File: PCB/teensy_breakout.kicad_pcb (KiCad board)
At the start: 2 copper layers, 88 x 68 mm, 59 parts, among them J1 Conn_01x02_Male, J10 3-way_power_jumper, J11 3-way_power_jumper, J12 Conn_01x06_Male, J13 Conn_01x06_Male, J14 Conn_01x06_Male, J15 Conn_01x06_Male, J16 3-way_power_jumper, J17 3-way_power_jumper, J18 Conn_01x06_Male, J19 Conn_01x06_Male, J2 Conn_01x03_Male, J20 Conn_01x06_Male, J21 Conn_01x06_Male, J22 3-way_power_jumper, J23 3-way_power_jumper, J24 Conn_01x03_Male, J25 Conn_01x03_Male, J26 Conn_01x03_Male, J27 Conn_01x03_Male, J28 Conn_01x06_Male, J29 Conn_01x03_Male, J3 Conn_01x03_Male, J30 Conn_01x03_Male, J31 Conn_01x03_Male, J32 Conn_01x03_Male, J33 Conn_01x03_Male, J35 Conn_01x03_Male, J36 Conn_01x03_Male, J4 Conn_01x04_Male, J5 Conn_01x04_Male, J6 Conn_01x03_Male, J7 Conn_01x02_Male, J8 Conn_01x04_Male, J9 Conn_01x04_Male, U1 Teensy4.0, U2 Pololu_D24V22Fx

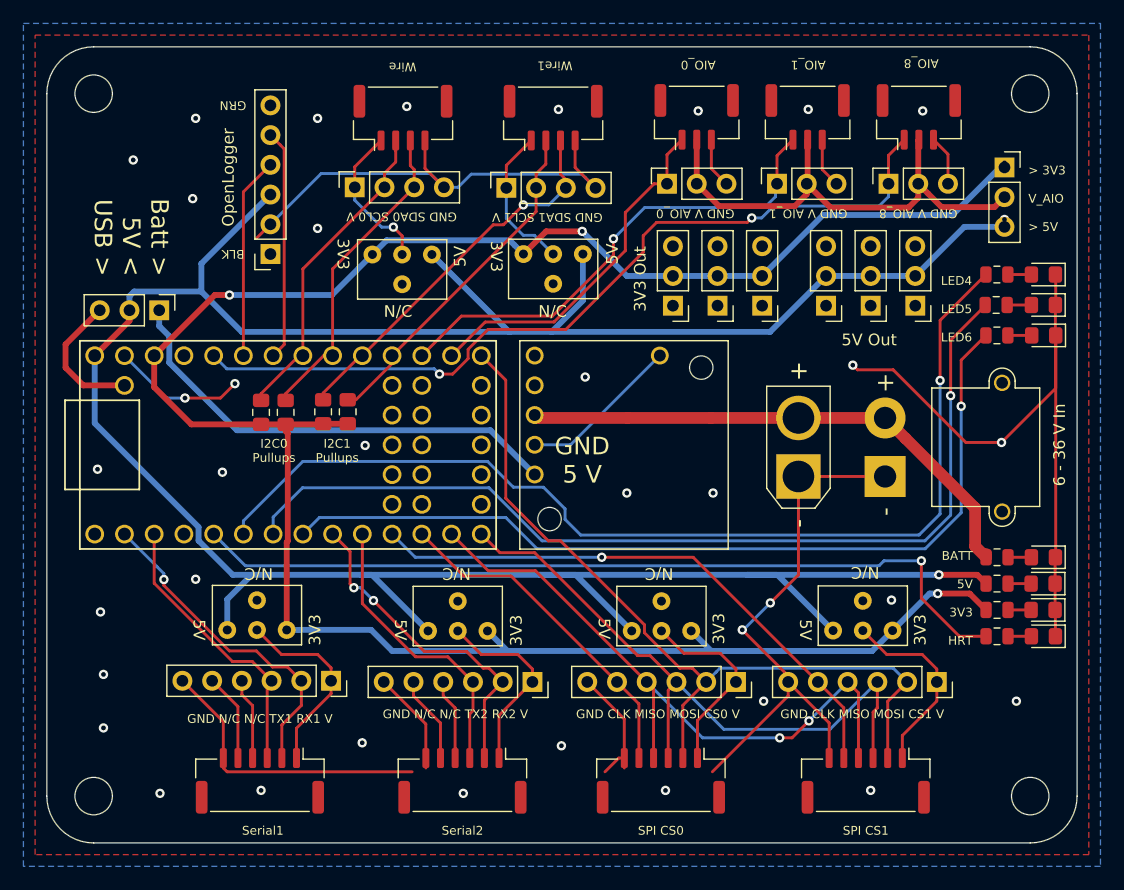
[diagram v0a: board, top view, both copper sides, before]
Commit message: Fixing all the paths
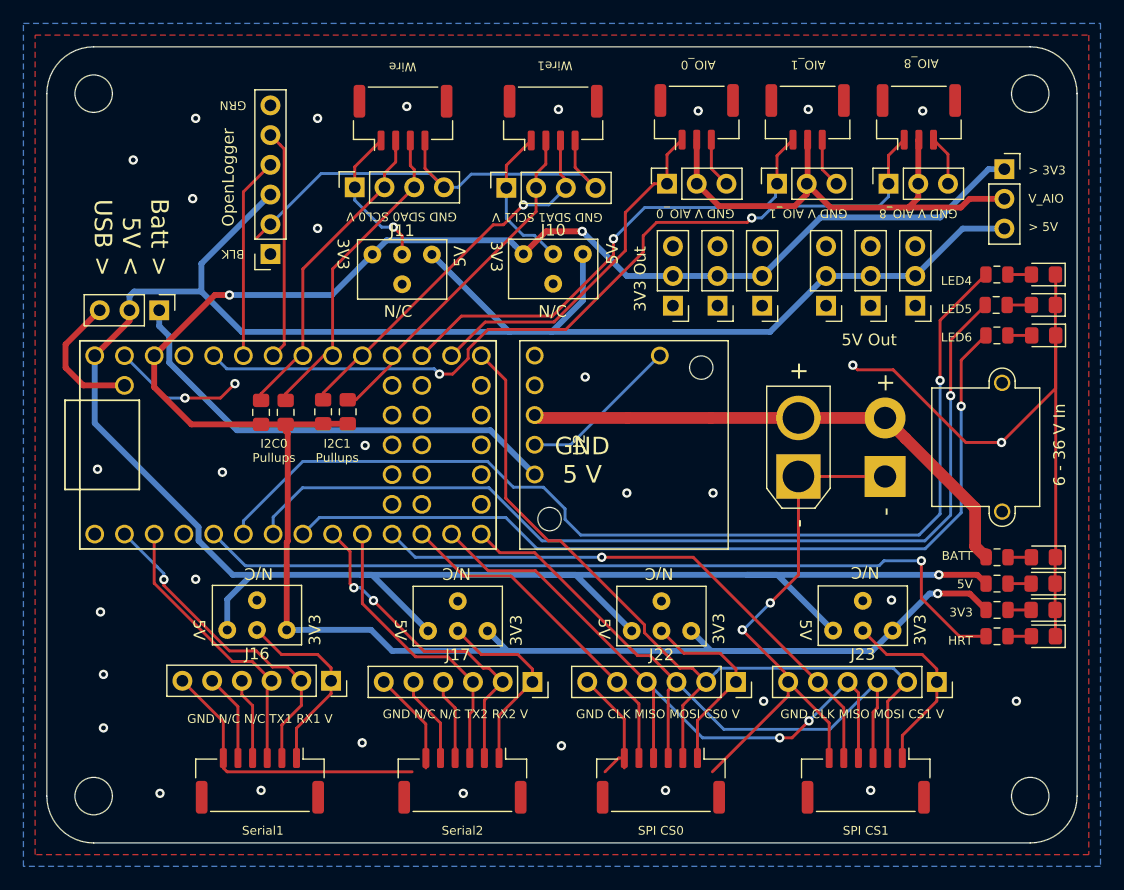
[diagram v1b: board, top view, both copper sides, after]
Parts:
- J10, J11, J16, J17, J22, J23: footprint ARCL:3-way_power_jumper -> other:3-way_power_jumper
- U2: footprint ARCL:Pololu_D24V22Fx_THT -> pololu:Pololu_D24V22Fx_THT
- moved J31 0.15 mm to (177.8, 106.4)
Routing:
- net +3V3: track 204.5 -> 204.3 mm, vias 4 -> 3
- net +5V: track 235.1 -> 235.0 mm, vias 2 -> 1

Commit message: Fixed the labelling on the SPI bus
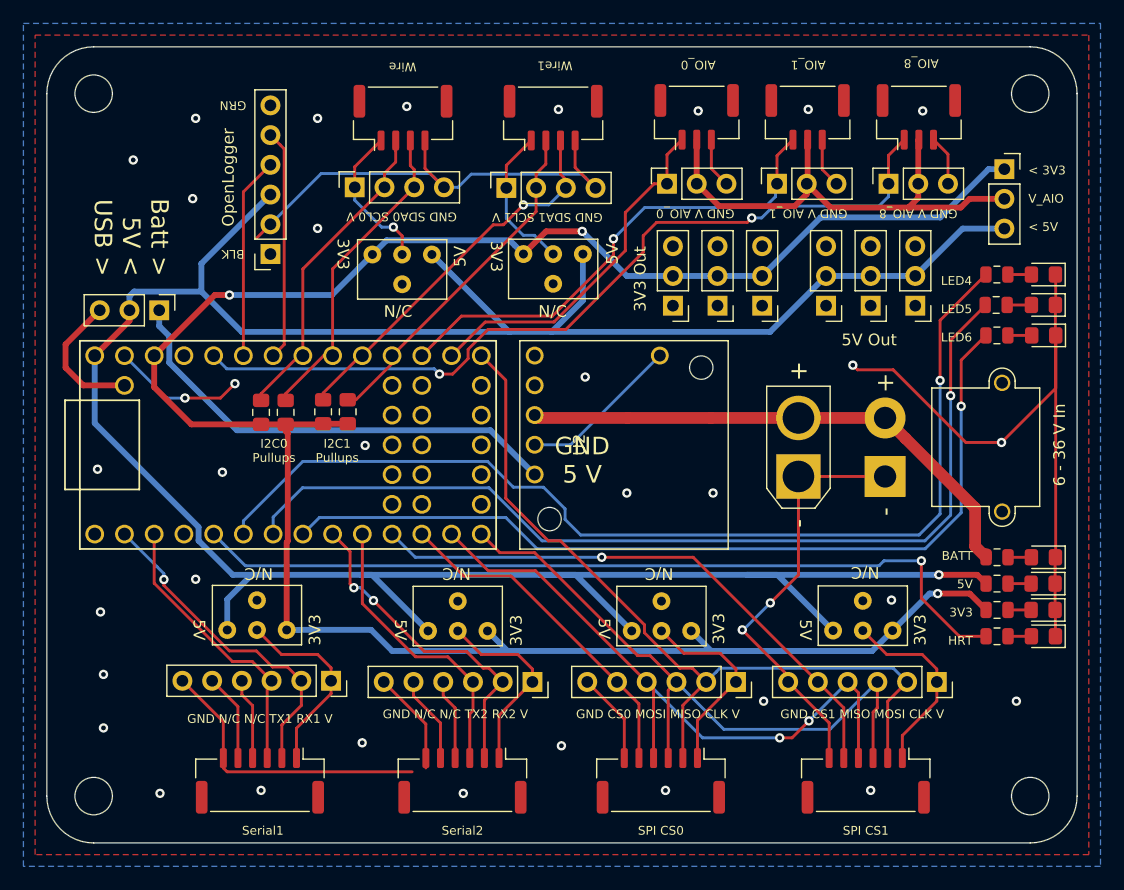
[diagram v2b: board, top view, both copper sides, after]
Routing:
- net Earth: track 229.4 -> 216.1 mm
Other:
- board text added: "< 3V3 V_AIO < 5V"
- board text added: "GND CS0 MOSI MISO CLK V"
- board text added: "GND CS1 MISO MOSI CLK V"
- board text removed: "> 3V3 V_AIO > 5V"
- board text removed: "GND CLK MISO MOSI CS0 V"
- board text removed: "GND CLK MISO MOSI CS1 V"
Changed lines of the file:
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@@
     (thickness 1.6)
     (drawings 62)
-    (tracks 516)
+    (tracks 511)
     (zones 0)
     (modules 59)
@@
     (add_net "Net-(D8-Pad2)")
     (add_net "Net-(J10-Pad1)")
-    (add_net "Net-(J10-Pad3)")
     (add_net "Net-(J11-Pad1)")
-    (add_net "Net-(J11-Pad3)")
     (add_net "Net-(J12-Pad1)")
     (add_net "Net-(J12-Pad4)")
@@
     (add_net "Net-(J13-Pad4)")
     (add_net "Net-(J13-Pad5)")
-    (add_net "Net-(J16-Pad3)")
-    (add_net "Net-(J17-Pad3)")
     (add_net "Net-(J18-Pad1)")
     (add_net "Net-(J19-Pad1)")
-    (add_net "Net-(J22-Pad3)")
-    (add_net "Net-(J23-Pad3)")
-    (add_net "Net-(J28-Pad1)")
-    (add_net "Net-(J28-Pad6)")
-    (add_net "Net-(U1-Pad1)")
-    (add_net "Net-(U1-Pad15)")
-    (add_net "Net-(U1-Pad16)")
-    (add_net "Net-(U1-Pad17)")
-    (add_net "Net-(U1-Pad18)")
-    (add_net "Net-(U1-Pad19)")
-    (add_net "Net-(U1-Pad30)")
-    (add_net "Net-(U1-Pad35)")
-    (add_net "Net-(U1-Pad36)")
-    (add_net "Net-(U1-Pad37)")
-    (add_net "Net-(U1-Pad38)")
-    (add_net "Net-(U1-Pad39)")
-    (add_net "Net-(U1-Pad4)")
-    (add_net "Net-(U1-Pad40)")
-    (add_net "Net-(U1-Pad41)")
-    (add_net "Net-(U1-Pad42)")
-    (add_net "Net-(U1-Pad43)")
-    (add_net "Net-(U1-Pad44)")
-    (add_net "Net-(U2-Pad2)")
-    (add_net "Net-(U2-Pad3)")
     (add_net SPI0_CLK)
     (add_net SPI0_CS0)
@@
   (module other:3-way_power_jumper (layer F.Cu)
     (at 165.7 148.4 180)
-    (fp_text reference J23 (at 0 0.5) (layer F.SilkS)
+    (fp_text reference J23 (at 0 0.5) (layer F.Fab)
       (effects (font (size 1 1) (thickness 0.15)))
     )
@@
   (module other:3-way_power_jumper (layer F.Cu)
     (at 148.5 148.43 180)
-    (fp_text reference J22 (at 0 0.5) (layer F.SilkS)
+    (fp_text reference J22 (at 0 0.5) (layer F.Fab)
       (effects (font (size 1 1) (thickness 0.15)))
     )
@@
   (module other:3-way_power_jumper (layer F.Cu)
     (at 131.1 148.43 180)
-    (fp_text reference J17 (at 0 0.5) (layer F.SilkS)
+    (fp_text reference J17 (at 0 0.5) (layer F.Fab)
       (effects (font (size 1 1) (thickness 0.15)))
     )
@@
   (module other:3-way_power_jumper (layer F.Cu)
     (at 113.95 148.35 180)
-    (fp_text reference J16 (at 0 0.5) (layer F.SilkS)
+    (fp_text reference J16 (at 0 0.5) (layer F.Fab)
       (effects (font (size 1 1) (thickness 0.15)))
     )
@@
   (module other:3-way_power_jumper (layer F.Cu)
     (at 126.35 111.2)
-    (fp_text reference J11 (at 0 0.5) (layer F.SilkS)
+    (fp_text reference J11 (at 0 0.5) (layer F.Fab)
       (effects (font (size 1 1) (thickness 0.15)))
     )
@@
   (module other:3-way_power_jumper (layer F.Cu)
     (at 139.25 111.16)
-    (fp_text reference J10 (at 0 0.5) (layer F.SilkS)
+    (fp_text reference J10 (at 0 0.5) (layer F.Fab)
       (effects (font (size 1 1) (thickness 0.15)))
     )
@@
     (effects (font (size 0.75 0.75) (thickness 0.15)))
   )
-  (gr_text "> 3V3\n\nV_AIO\n\n> 5V" (at 179.832 108.966) (layer F.SilkS)
+  (gr_text "< 3V3\n\nV_AIO\n\n< 5V" (at 179.832 108.966) (layer F.SilkS)
     (effects (font (size 0.75 0.75) (thickness 0.15)) (justify left))
   )
@@
     (effects (font (size 1 1) (thickness 0.2)))
   )
-  (gr_text "GND CLK MISO MOSI CS1 V" (at 165.65 153) (layer F.SilkS)
+  (gr_text "GND CS1 MISO MOSI CLK V" (at 165.65 153) (layer F.SilkS)
     (effects (font (size 0.75 0.75) (thickness 0.15)))
   )
-  (gr_text "GND CLK MISO MOSI CS0 V" (at 148.2 153) (layer F.SilkS)
+  (gr_text "GND CS0 MOSI MISO CLK V" (at 148.2 153) (layer F.SilkS)
     (effects (font (size 0.75 0.75) (thickness 0.15)))
   )
@@
   (segment (start 159.32 149.72) (end 159.32 150.25) (width 0.25) (layer F.Cu) (net 1))
   (segment (start 155.4 145.8) (end 159.32 149.72) (width 0.25) (layer F.Cu) (net 1))
-  (segment (start 145.325 157.6) (end 145.325 156.75) (width 0.25) (layer F.Cu) (net 1))
-  (segment (start 159.32 151.452081) (end 152.847071 157.92501) (width 0.25) (layer F.Cu) (net 1))
-  (segment (start 159.32 150.25) (end 159.32 151.452081) (width 0.25) (layer F.Cu) (net 1))
-  (segment (start 145.325 156.75) (end 144.85 156.75) (width 0.25) (layer F.Cu) (net 1))
   (segment (start 128.375 157.6) (end 128.375 156.75) (width 0.25) (layer F.Cu) (net 1))
-  (segment (start 144.85 156.75) (end 143.67499 157.92501) (width 0.25) (layer F.Cu) (net 1))
   (segment (start 111.075 157.6) (end 111.075 156.75) (width 0.25) (layer F.Cu) (net 1))
   (segment (start 111.40001 157.92501) (end 111.075 157.6) (width 0.25) (layer F.Cu) (net 1))

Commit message: Updated the version number
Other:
- board text added: "Teensy Breakout - v1.1a Matt Anderson 2021"
- board text removed: "Teensy Breakout - v1.1 Matt Anderson 2021"
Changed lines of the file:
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@@
       (drillshape 0)
       (scaleselection 1)
-      (outputdirectory ""))
+      (outputdirectory "outputs/"))
   )
   (net 0 "")
@@
     (effects (font (size 1.5 1.5) (thickness 0.3)))
   )
-  (gr_text "Teensy Breakout - v1.1\nMatt Anderson 2021" (at 175.006 160.147) (layer B.SilkS)
+  (gr_text "Teensy Breakout - v1.1a\nMatt Anderson 2021" (at 175.006 160.147) (layer B.SilkS)
     (effects (font (size 1.5 1.5) (thickness 0.3)) (justify left mirror))
   )
